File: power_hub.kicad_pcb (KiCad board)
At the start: 2 copper layers, 61 x 59 mm, 21 parts, among them Q1 SM4185

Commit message: v2
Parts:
- removed R3: 1K, Resistor_SMD:R_2010_5025Metric_Pad1.40x2.65mm_HandSolder
- removed xt60-male1: Conn_01x02_Pin, Connector_AMASS:AMASS_XT60-M_1x02_P7.20mm_Vertical
- added D3: D, Diode_SMD:D_SMA, F.Cu at (59.0, 64.5)
- added F1: Polyfuse, Fuse:Fuse_Bourns_MF-SM_7.98x5.44mm, F.Cu at (35.5, 23.2)
- added F2: Polyfuse, Fuse:Fuse_Bourns_MF-SM_7.98x5.44mm, F.Cu at (42.0, 23.2)
- added F3: Polyfuse, Fuse:Fuse_Bourns_MF-SM_7.98x5.44mm, F.Cu at (71.0, 23.2)
- added F4: Polyfuse, Fuse:Fuse_Bourns_MF-SM_7.98x5.44mm, F.Cu at (64.5, 23.2)
- added LED1: GREEN, LED_SMD:LED_0805_2012Metric, F.Cu at (22.1, 62.5)
- added LED2: GREEN, LED_SMD:LED_0805_2012Metric, F.Cu at (80.5, 42.4)
- added ON/OFF1: Conn_01x02_Pin, Connector_JST:JST_XH_B2B-XH-AM_1x02_P2.50mm_Vertical, F.Cu at (20.0, 36.2)
- added Q3: SM4185, Package_TO_SOT_SMD:TO-252-2, F.Cu at (40.0, 45.8)
- added Q4: 2N7002, Package_TO_SOT_SMD:SOT-23, F.Cu at (31.4, 37.5)
- added Q5: 2N7002, Package_TO_SOT_SMD:SOT-23, F.Cu at (32.6, 48.5)
- added Q6: SM4185, Package_TO_SOT_SMD:TO-252-2, F.Cu at (63.5, 48.0)
- added R11: 10k, Resistor_SMD:R_2010_5025Metric_Pad1.40x2.65mm_HandSolder, F.Cu at (38.5, 37.1)
- added R7: 5.1k, Resistor_SMD:R_2010_5025Metric_Pad1.40x2.65mm_HandSolder, F.Cu at (20.0, 56.6)
- added R8: 100R, Resistor_SMD:R_2010_5025Metric_Pad1.40x2.65mm_HandSolder, F.Cu at (28.0, 33.0)
- added R9: 100R, Resistor_SMD:R_2010_5025Metric_Pad1.40x2.65mm_HandSolder, F.Cu at (28.6, 44.5)
- added xt60-female3: Conn_01x02_Pin, Connector_AMASS:AMASS_XT60-M_1x02_P7.20mm_Vertical, F.Cu at (53.5, 27.0)
- Q1: value SM4185 -> 2N7002; footprint Package_TO_SOT_SMD:TO-252-2 -> Package_TO_SOT_SMD:SOT-23
- R2: value 100R -> 5.1k
- xt60-female1, xt60-female2: footprint Connector_AMASS:AMASS_XT60-F_1x02_P7.20mm_Vertical -> Connector_AMASS:AMASS_XT60-M_1x02_P7.20mm_Vertical
- moved H4 80.0 mm to (100.0, 20.0)
- moved xt30-female4 74.1 mm to (92.5, 67.2), turned to 90 degrees
- moved xt30-female3 68.8 mm to (85.0, 67.2), turned to 90 degrees
- moved xt30-female2 64.9 mm to (77.0, 67.5), turned to 90 degrees
- moved xt30-female1 62.4 mm to (69.0, 67.5), turned to 90 degrees
- moved H1 50.0 mm to (20.0, 20.0)
- moved xt60-female1 44.5 mm to (89.5, 38.8)
- moved xt60-female2 43.1 mm to (99.5, 38.8)
- moved xt30-motor4 38.3 mm to (29.5, 67.5), turned to 90 degrees
- moved R2 35.4 mm to (80.5, 36.6), turned to 90 degrees
- moved xt30-motor3 32.7 mm to (37.5, 67.5), turned to 90 degrees
- moved xt30-motor1 32.2 mm to (53.5, 67.5), turned to 90 degrees
- moved xt30-motor2 30.4 mm to (45.5, 67.5), turned to 90 degrees
- moved H2 30.0 mm to (100.0, 70.0)
- moved R1 28.9 mm to (64.5, 37.6), turned to -90 degrees
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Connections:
- AU1 pad 1: Net-(AU1-Pin_1) -> GND
- AU1 pad 2: GND -> Net-(AU1-Pin_2)
- D1 pad 1: 24v -> Vbat_2
- Q1 pad 1: Vbat -> ON/OFF
- Q1 pad 2: Net-(Q1-G) -> GND
- Q1 pad 3: 24v -> Net-(Q1-D)
- R1 pad 1: Vbat -> /24V_2
- R1 pad 2: Net-(Q1-G) -> Net-(Q1-D)
- R2 pad 1: Net-(Q1-G) -> Net-(LED2-K)
- R2 pad 2: Net-(AU1-Pin_1) -> GND
- xt30-female1 pad 2: Vbat -> Vbat_2
- xt30-female2 pad 2: Vbat -> Vbat_2
- xt30-female3 pad 2: Vbat -> Vbat_2
- xt30-female4 pad 2: Vbat -> Vbat_2
- xt30-motor1 pad 2: 24v -> Vbat_1
- xt30-motor2 pad 2: 24v -> Vbat_1
- xt30-motor3 pad 2: 24v -> Vbat_1
- xt30-motor4 pad 2: 24v -> Vbat_1
- xt60-female1 pad 2: Vbat -> Vbat_2
- xt60-female2 pad 2: Vbat -> Vbat_2
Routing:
- net ON/OFF: track 0.00 -> 34.7 mm, vias 0 -> 2
- net GND: track 5.95 -> 30.2 mm, vias 0 -> 1
- net Net-(Q1-D): track 0.00 -> 13.9 mm
- net Net-(AU1-Pin_1): track 12.0 -> 0.00 mm
- net Net-(Q4-S): track 0.00 -> 11.2 mm
- net Net-(Q1-G): track 10.9 -> 0.00 mm
- net Net-(Q3-G): track 0.00 -> 8.28 mm
- net Net-(AU1-Pin_2): track 0.00 -> 7.16 mm
- net Net-(ON/OFF1-Pin_2): track 0.00 -> 5.94 mm
- net Net-(LED1-K): track 0.00 -> 4.33 mm
- net AU: track 0.00 -> 3.31 mm
- net Net-(LED2-K): track 0.00 -> 2.77 mm
- net Vbat: track 0.85 -> 0.00 mm
- net Vbat_2: track 0.00 -> 0.71 mm
- net /24V_2: track 0.00 -> 0.71 mm
- added copper zone on F.Cu, net /24V_1
- added copper zone on F.Cu, net /24V_2
- added copper zone on F.Cu, net GND
- added copper zone on F.Cu, net V_IN
- added copper zone on F.Cu, net Vbat_1
- added copper zone on F.Cu, net Vbat_2
- removed copper zone on F.Cu, net 24v
- removed copper zone on F.Cu, net Vbat
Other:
- board size 61 x 59 mm -> 89.5 x 58.5 mm
- board text added: "Team Opossum Power_hub v1"

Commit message: fix issue
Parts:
- removed H3, H4: MountingHole_Pad, MountingHole:MountingHole_3.2mm_M3_DIN965_Pad
- added D2: BZT52C15S, Diode_SMD:D_SOD-323, F.Cu at (57.5, 47.5)
- added D4: BZT52C15S, Diode_SMD:D_SOD-323, F.Cu at (67.5, 47.9)
- added R3: 10k, Resistor_SMD:R_0805_2012Metric_Pad1.20x1.40mm_HandSolder, F.Cu at (41.0, 53.2)
- added R4: 10k, Resistor_SMD:R_0805_2012Metric_Pad1.20x1.40mm_HandSolder, F.Cu at (38.5, 47.2)
- added R5: 10k, Resistor_SMD:R_0805_2012Metric_Pad1.20x1.40mm_HandSolder, F.Cu at (73.0, 51.0)
- R1, R11, R2, R7, R8, R9: footprint Resistor_SMD:R_2010_5025Metric_Pad1.40x2.65mm_HandSolder -> Resistor_SMD:R_0805_2012Metric_Pad1.20x1.40mm_HandSolder
- moved H2 41.2 mm to (90.0, 30.0), turned to 90 degrees
- moved D1 30.5 mm to (94.0, 66.2)
- moved D3 30.0 mm to (29.0, 66.2)
- moved xt30-motor4 27.6 mm to (57.0, 69.2)
- moved R11 20.7 mm to (57.5, 45.2), turned to 0 degrees
- moved LED1 20.1 mm to (41.6, 57.7)
- moved xt30-motor1 19.1 mm to (34.5, 69.2)
- moved Q3 18.6 mm to (56.0, 55.3), turned to -90 degrees
- moved R7 18.0 mm to (38.0, 56.7)
- moved Q1 17.4 mm to (73.0, 47.0), turned to 90 degrees
- moved xt60-female2 16.1 mm to (92.6, 53.4), turned to 180 degrees
- moved F1 15.8 mm to (46.0, 35.0)
- moved ON/OFF1 14.8 mm to (30.5, 46.7)
- moved R8 14.8 mm to (37.6, 44.2)
- moved Q4 14.6 mm to (43.1, 46.3)
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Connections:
- Q1 pad 3: Net-(Q1-D) -> Net-(D4-A)
- Q3 pad 1: Vbat_1 -> Net-(D2-A)
- Q3 pad 2: Net-(Q3-G) -> Vbat_1
- Q4 pad 3: Net-(Q3-G) -> Net-(D2-A)
- Q6 pad 1: Vbat_2 -> Net-(D4-A)
- Q6 pad 2: Net-(Q1-D) -> Vbat_2
- R1 pad 2: Net-(Q1-D) -> Net-(D4-A)
- R11 pad 2: Net-(Q3-G) -> Net-(D2-A)
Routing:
- net Net-(D2-A): track 0.00 -> 23.1 mm, vias 0 -> 2
- net Net-(Q1-D): track 13.9 -> 0.00 mm
- net Net-(D4-A): track 0.00 -> 10.9 mm
- net Net-(Q3-G): track 8.28 -> 0.00 mm
- net ON/OFF: track 34.7 -> 41.6 mm
- net GND: track 30.2 -> 24.2 mm, vias 1 -> 2
- net AU: track 3.31 -> 5.65 mm
- net Net-(LED1-K): track 4.33 -> 2.62 mm
- net Vbat_2: track 0.71 -> 0.00 mm
- net /24V_2: track 0.71 -> 0.07 mm
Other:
- board size 89.5 x 58.5 mm -> 70.5 x 48 mm
- board text removed: "Team Opossum Power_hub v1"

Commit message: reprise v2
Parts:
- added D5: BZT52C15S, Diode_SMD:D_SOD-323, F.Cu at (57.3, 56.5)
- added D6: D, Diode_SMD:D_SMA, F.Cu at (64.0, 51.9)
- added F5: Polyfuse, Fuse:Fuse_Bourns_MF-SM_7.98x5.44mm, F.Cu at (63.6, 68.0)
- added F6: Polyfuse, Fuse:Fuse_Bourns_MF-SM_7.98x5.44mm, F.Cu at (70.6, 68.0)
- added H3: MountingHole_Pad, MountingHole:MountingHole_3.2mm_M3_DIN965_Pad, F.Cu at (102.0, 70.0)
- added H4: MountingHole_Pad, MountingHole:MountingHole_3.2mm_M3_DIN965_Pad, F.Cu at (24.0, 70.0)
- added LED3: GREEN, LED_SMD:LED_0805_2012Metric, F.Cu at (55.2, 51.6)
- added Q8: SM4185, Package_TO_SOT_SMD:TO-252-2, F.Cu at (66.9, 57.7)
- added R12: 10k, Resistor_SMD:R_0805_2012Metric_Pad1.20x1.40mm_HandSolder, F.Cu at (59.4, 56.5)
- added R13: 5.1k, Resistor_SMD:R_0805_2012Metric_Pad1.20x1.40mm_HandSolder, F.Cu at (58.1, 50.7)
- added xt30-motor5: Conn_01x02_Pin, Connector_AMASS:AMASS_XT30U-F_1x02_P5.0mm_Vertical, F.Cu at (61.3, 24.8)
- added xt30-motor6: Conn_01x02_Pin, Connector_AMASS:AMASS_XT30U-F_1x02_P5.0mm_Vertical, F.Cu at (61.3, 31.4)
- added xt30-motor7: Conn_01x02_Pin, Connector_AMASS:AMASS_XT30U-F_1x02_P5.0mm_Vertical, F.Cu at (61.3, 37.9)
- added xt30-motor8: Conn_01x02_Pin, Connector_AMASS:AMASS_XT30U-F_1x02_P5.0mm_Vertical, F.Cu at (61.3, 44.4)
- moved xt30-motor4 46.7 mm to (44.1, 24.3), turned to 0 degrees
- moved xt30-female1 46.3 mm to (80.5, 25.1), turned to 0 degrees
- moved xt30-motor3 38.8 mm to (44.1, 30.8), turned to 0 degrees
- moved F4 37.8 mm to (91.1, 68.2), turned to 90 degrees
- moved xt30-female3 37.6 mm to (80.5, 31.6), turned to 0 degrees
- moved F3 37.6 mm to (84.1, 68.2), turned to 90 degrees
- moved R7 35.4 mm to (73.4, 55.3), turned to -90 degrees
- moved F2 33.9 mm to (47.3, 67.9), turned to 90 degrees
- moved F1 33.4 mm to (40.3, 67.9), turned to 90 degrees
- moved xt60-female3 33.2 mm to (32.4, 61.1), turned to -90 degrees
- moved xt30-motor2 32.0 mm to (44.1, 37.3), turned to 0 degrees
- moved xt30-female2 31.9 mm to (80.5, 38.1), turned to 0 degrees
- moved LED1 31.0 mm to (72.1, 52.3), turned to 180 degrees
- moved xt30-motor1 27.2 mm to (44.1, 43.8), turned to 0 degrees
- moved xt30-female4 25.6 mm to (80.5, 44.7), turned to 0 degrees
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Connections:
- net /24V_2 renamed /24V_3
- net Net-(D2-A) renamed /on/off/au
- D3 pad 1: Vbat_1 -> V_moteurs
- Q3 pad 2: Vbat_1 -> V_moteurs
- xt30-motor1 pad 2: Vbat_1 -> V_moteurs
- xt30-motor2 pad 2: Vbat_1 -> V_moteurs
- xt30-motor3 pad 2: Vbat_1 -> V_moteurs
- xt30-motor4 pad 2: Vbat_1 -> V_moteurs
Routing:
- net /on/off/au: track 23.1 -> 58.0 mm
- net ON/OFF: track 41.6 -> 69.6 mm
- net GND: track 24.2 -> 16.3 mm, vias 2 -> 22
- net Net-(D4-A): track 10.9 -> 5.59 mm
- net Net-(Q4-S): track 11.6 -> 8.54 mm
- net Net-(AU1-Pin_2): track 6.83 -> 4.04 mm
- net Net-(LED3-K): track 0.00 -> 2.00 mm
- net Net-(ON/OFF1-Pin_2): track 6.15 -> 4.15 mm
- net Net-(LED2-K): track 2.73 -> 1.86 mm
- net AU: track 5.65 -> 4.96 mm
- added copper zone on F.Cu, net /24V_2
- added copper zone on F.Cu, net V_moteurs
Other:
- board size 70.5 x 48 mm -> 86 x 54 mm
- board text added: "DC-DC"
- board text added: "Motors"
- board text added: "Others"
- board text added: "V_IN - 24V"
- board text added: "power_hub Opossums 2024"

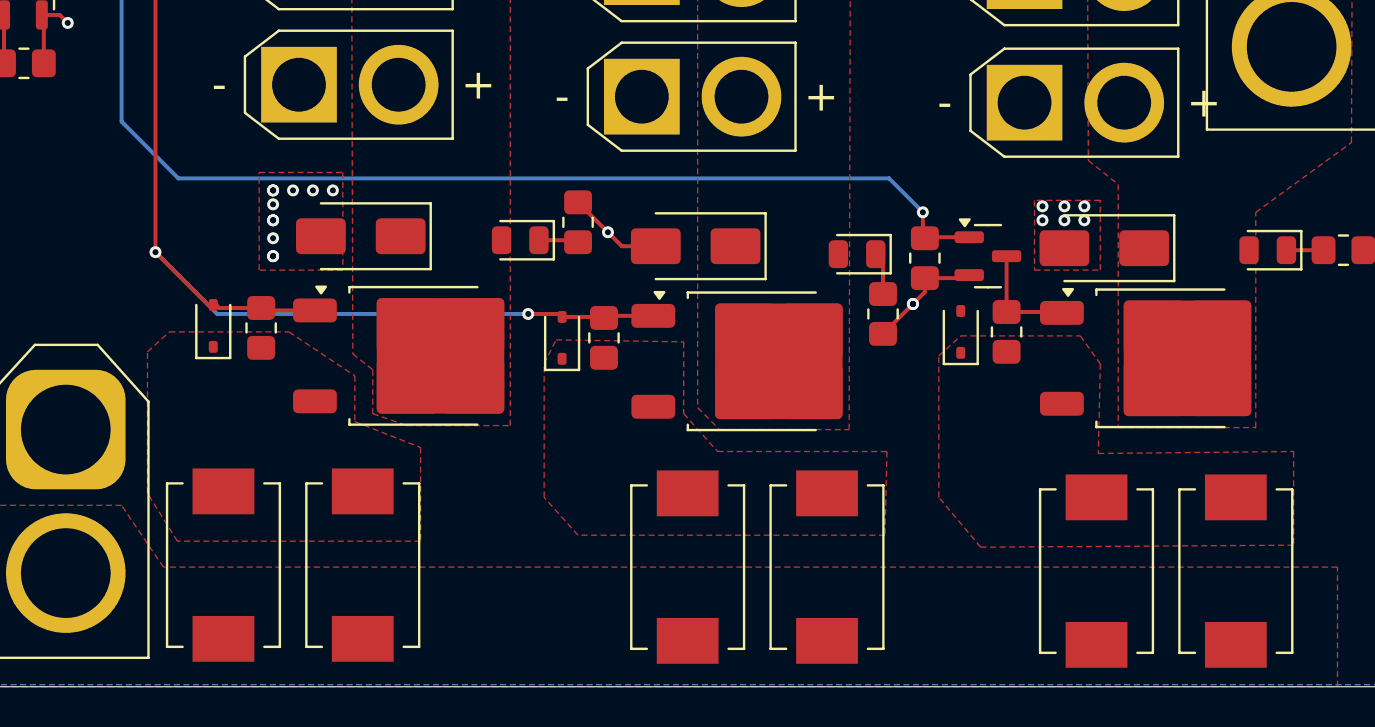
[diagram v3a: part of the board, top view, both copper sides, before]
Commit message: update schematic and footprint, still a diode to choose
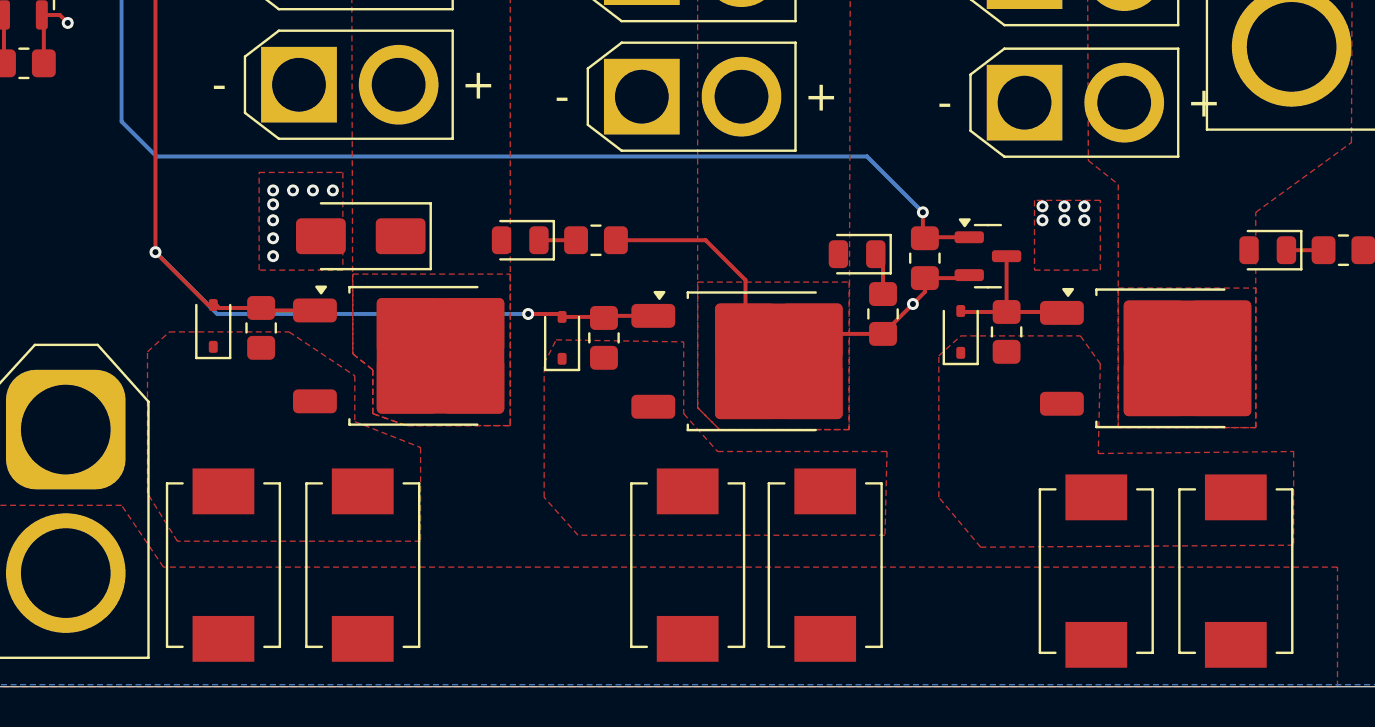
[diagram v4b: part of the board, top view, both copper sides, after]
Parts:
- removed D1, D6: D, Diode_SMD:D_SMA
- removed F3, F4, F5, F6: Polyfuse, Fuse:Fuse_Bourns_MF-SM_7.98x5.44mm
- added F10: SMD1812-150C-33V 1812_SERI, Fuse:Fuse_Bourns_MF-SM_7.98x5.44mm, F.Cu at (91.1, 68.2)
- added F7: SMD1812-150C-33V 1812_SERI, Fuse:Fuse_Bourns_MF-SM_7.98x5.44mm, F.Cu at (63.6, 67.9)
- added F8: SMD1812-150C-33V 1812_SERI, Fuse:Fuse_Bourns_MF-SM_7.98x5.44mm, F.Cu at (70.5, 67.9)
- added F9: SMD1812-150C-33V 1812_SERI, Fuse:Fuse_Bourns_MF-SM_7.98x5.44mm, F.Cu at (84.1, 68.2)
- F1, F2: value Polyfuse -> SMD1812-150C-33V 1812_SERI
- moved R13 1.27 mm to (59.0, 51.6), turned to 0 degrees
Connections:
- AU1 pad 1: GND -> Vbat_1
- D3 pad 2: GND -> Vbat_1
- H1 pad 1: GND -> Vbat_1
- H2 pad 1: GND -> Vbat_1
- H3 pad 1: GND -> Vbat_1
- H4 pad 1: GND -> Vbat_1
- LED2 pad 2: Vbat_2 -> Vbat_1
- ON/OFF1 pad 1: GND -> Vbat_1
- Q1 pad 2: GND -> Vbat_1
- Q5 pad 2: GND -> Vbat_1
- Q6 pad 2: Vbat_2 -> Vbat_1
- R13 pad 2: GND -> Vbat_1
- R2 pad 2: GND -> Vbat_1
- R3 pad 2: GND -> Vbat_1
- R5 pad 2: GND -> Vbat_1
- R7 pad 2: GND -> Vbat_1
- xt30-female1 pad 1: GND -> Vbat_1
- xt30-female1 pad 2: Vbat_2 -> Vbat_1
- xt30-female2 pad 1: GND -> Vbat_1
- xt30-female2 pad 2: Vbat_2 -> Vbat_1
- xt30-female3 pad 1: GND -> Vbat_1
- xt30-female3 pad 2: Vbat_2 -> Vbat_1
- xt30-female4 pad 1: GND -> Vbat_1
- xt30-female4 pad 2: Vbat_2 -> Vbat_1
- xt30-motor1 pad 1: GND -> Vbat_1
- xt30-motor2 pad 1: GND -> Vbat_1
- xt30-motor3 pad 1: GND -> Vbat_1
- xt30-motor4 pad 1: GND -> Vbat_1
- xt30-motor5 pad 1: GND -> Vbat_1
- xt30-motor6 pad 1: GND -> Vbat_1
- xt30-motor7 pad 1: GND -> Vbat_1
- xt30-motor8 pad 1: GND -> Vbat_1
- xt60-female1 pad 1: GND -> Vbat_1
- xt60-female1 pad 2: Vbat_2 -> Vbat_1
- xt60-female2 pad 1: GND -> Vbat_1
- xt60-female2 pad 2: Vbat_2 -> Vbat_1
- xt60-female3 pad 1: GND -> Vbat_1
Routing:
- net Vbat_1: track 0.00 -> 25.0 mm, vias 0 -> 17
- net GND: track 16.3 -> 0.00 mm, vias 22 -> 0
- net Net-(D4-A): track 5.59 -> 7.91 mm
- added copper zone on B.Cu, net Vbat_1
- removed copper zone on B.Cu, net GND
- removed copper zone on F.Cu, net GND
- removed copper zone on F.Cu, net Vbat_2

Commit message: update all
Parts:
- removed F10, F7: SMD1812-150C-33V 1812_SERI, Fuse:Fuse_Bourns_MF-SM_7.98x5.44mm
- removed H1: MountingHole_Pad, MountingHole:MountingHole_3.2mm_M3_DIN965_Pad
- removed LED1, LED2, LED3: GREEN, LED_SMD:LED_0805_2012Metric
- removed R13, R2, R7: 5.1k, Resistor_SMD:R_0805_2012Metric_Pad1.20x1.40mm_HandSolder
- removed xt30-female4, xt30-motor8: Conn_01x02_Pin, Connector_AMASS:AMASS_XT30U-F_1x02_P5.0mm_Vertical
- removed xt60-female1, xt60-female2, xt60-female3: Conn_01x02_Pin, Connector_AMASS:AMASS_XT60-M_1x02_P7.20mm_Vertical
- added D1: D, Diode_SMD:D_SMA, F.Cu at (129.6, 106.7)
- added D6: D, Diode_SMD:D_SMA, F.Cu at (140.1, 106.8)
- added D7: D, Diode_SMD:D_SMA, F.Cu at (118.7, 106.7)
- added J1: Conn_01x02_Pin, Connector_AMASS:AMASS_XT60-M_1x02_P7.20mm_Vertical, F.Cu at (107.0, 138.1)
- added Q2: SM4185, Package_TO_SOT_SMD:TO-252-2, F.Cu at (124.7, 118.1)
- added Q7: SM4185, Package_TO_SOT_SMD:TO-252-2, F.Cu at (135.3, 118.1)
- added Q9: SM4185, Package_TO_SOT_SMD:TO-252-2, F.Cu at (114.0, 118.1)
- moved xt30-female1 147.2 mm to (181.0, 132.6), turned to 180 degrees
- moved xt30-female2 133.6 mm to (180.9, 126.2), turned to 180 degrees
- moved xt30-female3 133.6 mm to (180.8, 119.8), turned to 180 degrees
- moved xt30-motor5 129.6 mm to (163.6, 104.3), turned to -90 degrees
- moved xt30-motor7 127.5 mm to (170.2, 104.3), turned to -90 degrees
- moved Q4 124.9 mm to (112.4, 127.3)
- moved R4 124.9 mm to (109.4, 127.3)
- moved Q5 123.3 mm to (112.4, 131.3), turned to 0 degrees
- moved H2 122.9 mm to (142.5, 140.0)
- moved xt30-motor6 120.4 mm to (157.1, 104.3), turned to -90 degrees
- moved D5 119.5 mm to (154.3, 126.2)
- moved R3 118.8 mm to (109.4, 131.3), turned to -90 degrees
- moved xt30-motor1 118.6 mm to (145.9, 104.7), turned to -90 degrees
- moved Q6 118.4 mm to (172.9, 139.5)
- moved D3 117.6 mm to (150.9, 106.7), turned to 90 degrees
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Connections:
- AU1 pad 1: Vbat_1 -> GND
- D3 pad 1: V_moteurs -> V_moteurs_1
- D3 pad 2: Vbat_1 -> GND
- H2 pad 1: Vbat_1 -> GND
- H3 pad 1: Vbat_1 -> GND
- H4 pad 1: Vbat_1 -> GND
- ON/OFF1 pad 1: Vbat_1 -> GND
- Q1 pad 2: Vbat_1 -> GND
- Q3 pad 2: V_moteurs -> V_moteurs_1
- Q5 pad 2: Vbat_1 -> GND
- Q6 pad 2: Vbat_1 -> Vbat_2
- R3 pad 2: Vbat_1 -> GND
- R5 pad 2: Vbat_1 -> GND
- xt30-female1 pad 1: Vbat_1 -> GND
- xt30-female1 pad 2: Vbat_1 -> Vbat_2
- xt30-female2 pad 1: Vbat_1 -> GND
- xt30-female2 pad 2: Vbat_1 -> Vbat_2
- xt30-female3 pad 1: Vbat_1 -> GND
- xt30-female3 pad 2: Vbat_1 -> Vbat_2
- xt30-motor1 pad 1: Vbat_1 -> GND
- xt30-motor1 pad 2: V_moteurs -> V_moteurs_1
- xt30-motor2 pad 1: Vbat_1 -> GND
- xt30-motor2 pad 2: V_moteurs -> V_moteurs_2
- xt30-motor3 pad 1: Vbat_1 -> GND
- xt30-motor3 pad 2: V_moteurs -> V_moteurs_3
- xt30-motor4 pad 1: Vbat_1 -> GND
- xt30-motor4 pad 2: V_moteurs -> V_moteurs_4
- xt30-motor5 pad 1: Vbat_1 -> GND
- xt30-motor6 pad 1: Vbat_1 -> GND
- xt30-motor7 pad 1: Vbat_1 -> GND
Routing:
- net Vbat_1: track 25.0 -> 0.00 mm, vias 17 -> 0
- net ON/OFF: track 69.6 -> 84.6 mm
- net /on/off/au: track 58.0 -> 69.8 mm, vias 2 -> 6
- net Net-(AU1-Pin_2): track 4.04 -> 8.25 mm
- net Net-(ON/OFF1-Pin_2): track 4.15 -> 8.31 mm
- net AU: track 4.96 -> 8.00 mm
- net Net-(Q4-S): track 8.54 -> 6.33 mm
- net Net-(LED1-K): track 2.15 -> 0.00 mm
- net GND: track 0.00 -> 2.08 mm
- net Net-(LED3-K): track 2.00 -> 0.00 mm
- net Net-(LED2-K): track 1.86 -> 0.00 mm
- net Net-(D4-A): track 7.91 -> 7.27 mm
- added copper zone on B.Cu, net GND
- added copper zone on F.Cu, net GND
- added copper zone on F.Cu, net V_moteurs_1
- added copper zone on F.Cu, net V_moteurs_2
- added copper zone on F.Cu, net V_moteurs_3
- added copper zone on F.Cu, net V_moteurs_4
- added copper zone on F.Cu, net Vbat_2
- removed copper zone on F.Cu, net V_moteurs
- removed copper zone on B.Cu, net Vbat_1
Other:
- board size 86 x 54 mm -> 85 x 44 mm
- board text added: "Opossum - Power 2025"
- board text added: "Vin - 24V"
- board text added: "Warning NO AU"
- board text removed: "DC-DC"
- board text removed: "Motors"
- board text removed: "Others"
- board text removed: "V_IN - 24V"
- board text removed: "power_hub Opossums 2024"

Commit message: add serigraphy
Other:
- board text added: "POWER - OPOSSUM 2025"
- board text added: "POWER AU"
- board text added: "motor 1"
- board text added: "motor 2"
- board text added: "motor 3"
- board text removed: "Opossum - Power 2025"

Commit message: add readme
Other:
- board text added: "motor 4"
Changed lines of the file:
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@@
 	)
 	(gr_text "motor 1"
-		(at 120 123.05 90)
-		(layer "F.SilkS")
+		(at 120.15 123.975 90)
+		(layer "F.SilkS" knockout)
 		(effects
 			(font
@@
 	)
 	(gr_text "motor 3"
-		(at 141.5 122.85 90)
-		(layer "F.SilkS")
+		(at 141.95 123.925 90)
+		(layer "F.SilkS" knockout)
 		(effects
 			(font
@@
 	)
 	(gr_text "POWER \nAU"
-		(at 179.325 112.875 0)
-		(layer "F.SilkS")
+		(at 180.3 112.75 0)
+		(layer "F.SilkS" knockout)
 		(effects
 			(font
@@
 	)
 	(gr_text "motor 2"
-		(at 130.65 122.975 90)
-		(layer "F.SilkS")
+		(at 130.975 124.05 90)
+		(layer "F.SilkS" knockout)
 		(effects
 			(font
@@
 		)
 	)
-	(gr_text "motor 3"
-		(at 152.625 122.9 90)
-		(layer "F.SilkS")
+	(gr_text "motor 4"
+		(at 152.875 123.8 90)
+		(layer "F.SilkS" knockout)
 		(effects
 			(font
